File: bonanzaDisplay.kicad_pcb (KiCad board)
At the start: 6 copper layers, 61 x 101 mm, 81 parts, among them J1 OLED-1.31-SSD1322, J15 SWD, J2 Conn_01x02, J5 Conn_01x10, J6 USB_C_Receptacle_USB2.0, SW1 TS-1088-AR02016, SW2 TS-1088-AR02016, SW3 SIQ-02FVS3, U1 RP2354A, U2 XC6206P302MR, U3 XC6206P282MR, U4 TPS62933DRLR, Y1 ABM8-272-T3

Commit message: updated version to v3. switch to 12P FPC
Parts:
- J5: footprint bonanzaDisplay:FPC-SMD_10P-P1.0_FGS-XJ-H2.0 -> bonanzaDisplay:FPC-SMD_12P-P1.00_FGS-XJ-H2.0
- TP22: value SCL -> TX
- TP23: value SDA -> RX
- moved J5 0.97 mm to (118.8, 80.7)
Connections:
- net /DISP_SCL renamed /DISP_TX
- net /DISP_SDA renamed /DISP_RX
- J5 pad 11: GND -> /SWD-DISP
- J5 pad 12: GND -> /SWCLK
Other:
- board text added: "bonanzaDisplay v3"
- board text removed: "bonanzaDisplay v2"

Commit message: rough placements and critical routing done
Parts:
- added TP64: VBUS, bonanzaDisplay:TestPoint_Pad_D1.0mm, B.Cu at (124.5, 33.5)
- J2: moved to B.Cu
- J6: value USB_C_Receptacle_USB2.0 -> TYPE-C-31-M-12; footprint bonanzaDisplay:USB_C_Receptacle_GCT_USB4105-xx-A -> bonanzaDisplay:USB-C_SMD-TYPE-C-31-M-12_1
- moved SW1 84.8 mm to (145.6, 48.0), turned to -90 degrees
- moved R33 82.3 mm to (143.1, 48.1), turned to 90 degrees
- moved SW2 74.5 mm to (137.9, 47.9), turned to -90 degrees
- moved C31 52.6 mm to (136.0, 54.0), turned to 90 degrees
- moved C33 52.0 mm to (137.2, 54.0), turned to 90 degrees
- moved C28 51.3 mm to (140.4, 53.6), turned to 90 degrees
- moved C15 51.0 mm to (141.5, 53.6), turned to 90 degrees
- moved C25 50.5 mm to (143.1, 53.6), turned to 90 degrees
- moved C17 50.4 mm to (131.6, 57.7), turned to 180 degrees
- moved C18 50.3 mm to (144.2, 53.6), turned to 90 degrees
- moved R31 50.1 mm to (145.4, 53.6), turned to 90 degrees
- moved C20 49.8 mm to (133.3, 57.3), turned to 90 degrees
- moved TP17 49.1 mm to (146.9, 53.5), turned to -90 degrees
- moved Y1 47.0 mm to (131.7, 60.5), turned to 90 degrees
- moved L1 46.6 mm to (146.9, 56.0), turned to 90 degrees
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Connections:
- J5 pad 11: /SWD-DISP -> /SWD
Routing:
- net /SW_CCW: track 32.8 -> 82.9 mm, vias 0 -> 2
- net /SW_SW: track 34.0 -> 81.6 mm, vias 0 -> 2
- net /SW_CW: track 36.4 -> 78.0 mm, vias 0 -> 2
- net Net-(J1-IREF): track 2.45 -> 37.7 mm, vias 0 -> 2
- net Net-(J1-VDD): track 2.60 -> 37.1 mm, vias 0 -> 2
- net Net-(J1-VCI): track 2.44 -> 35.6 mm, vias 0 -> 2
- net /2V8: track 16.6 -> 49.2 mm
- net /12V: track 73.3 -> 42.8 mm, vias 5 -> 4
- net Net-(U1-~{QSPI_SS}): track 30.0 -> 0.00 mm, vias 2 -> 0
- net /3V0: track 15.1 -> 44.3 mm, vias 2 -> 4
- net Net-(J1-VSL): track 4.31 -> 33.4 mm, vias 0 -> 2
- net Net-(U1-RUN): track 28.2 -> 0.00 mm, vias 2 -> 0
- net /D6: track 13.1 -> 37.1 mm, vias 0 -> 2
- net /D7: track 13.0 -> 36.9 mm
- net /D5: track 13.1 -> 36.9 mm, vias 0 -> 2
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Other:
- board size 61 x 101 mm -> 30.1 x 89.5 mm

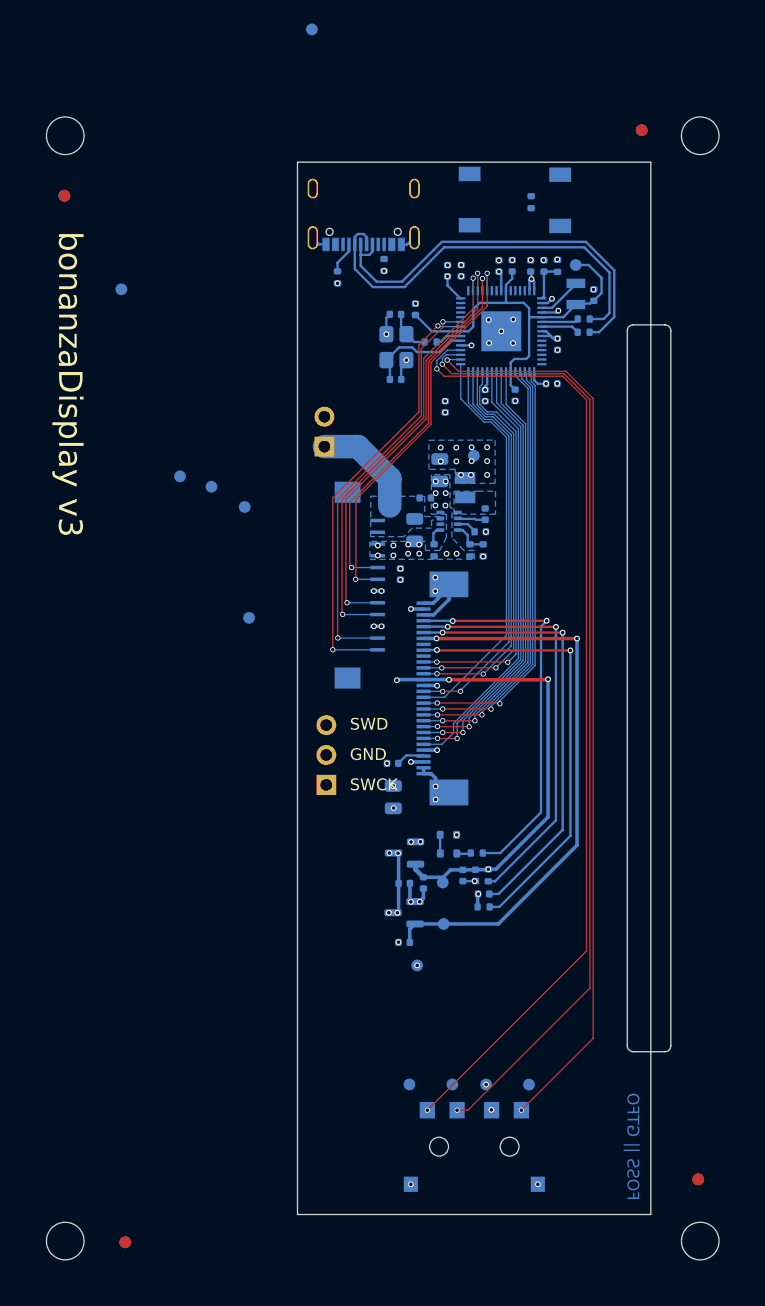
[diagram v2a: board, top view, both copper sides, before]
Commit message: finished routing, DRC and ERC pass
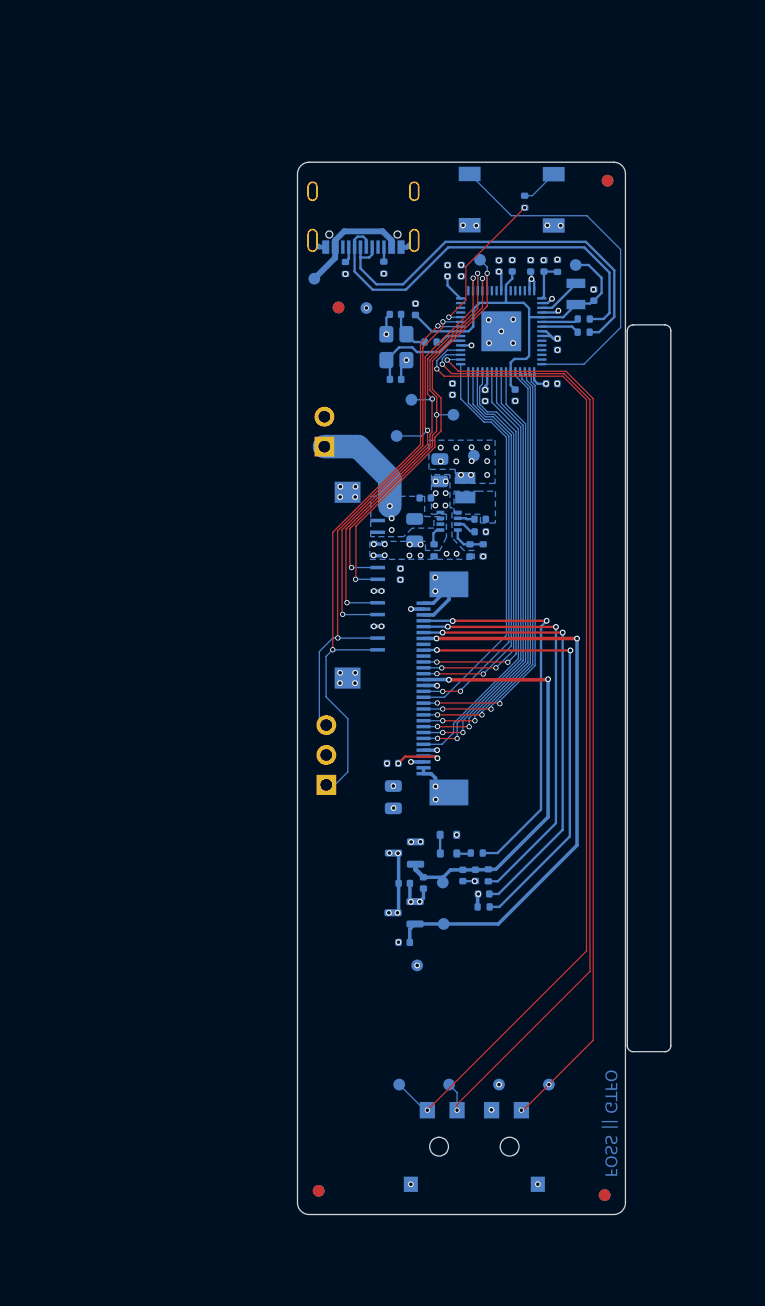
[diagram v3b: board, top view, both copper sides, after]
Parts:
- removed H1, H2, H3, H4: MountingHole_Pad, MountingHole:MountingHole_3.2mm_M3
- moved TP21 30.2 mm to (136.5, 66.2)
- moved TP20 29.0 mm to (138.8, 53.0)
- moved TP19 28.2 mm to (129.1, 57.1)
- moved FID1 25.2 mm to (126.7, 57.1)
- moved TP64 21.2 mm to (124.7, 54.7)
- moved TP23 18.7 mm to (131.7, 68.0), turned to 180 degrees
- moved TP22 18.5 mm to (132.9, 65.0), turned to 180 degrees
- moved FID4 17.0 mm to (125.0, 132.2)
- moved FID3 8.07 mm to (149.4, 132.6)
- moved FID2 5.19 mm to (149.6, 46.3)
- moved TP14 1.69 mm to (144.6, 123.2)
- moved C32 1.62 mm to (136.4, 64.0)
- moved TP24 1.10 mm to (140.4, 123.2)
- moved R2 1.04 mm to (127.3, 53.7)
- moved TP12 0.87 mm to (131.9, 123.2)
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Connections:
- J5 pad 14: unconnected-(J5-Pad14) -> GND
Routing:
- net Net-(U1-~{QSPI_SS}): track 0.00 -> 30.1 mm
- net /SWCLK: track 37.0 -> 50.7 mm
- net Net-(U1-RUN): track 0.00 -> 12.9 mm, vias 0 -> 2
- net Net-(J6-VBUS-PadA4B9): track 0.00 -> 10.0 mm
- net /SWD: track 35.5 -> 44.1 mm
- net /3V0: track 44.3 -> 36.5 mm, vias 4 -> 2
- net /12V: track 42.8 -> 37.1 mm, vias 4 -> 7
- net /SW_CCW: track 82.9 -> 86.2 mm
- net Net-(R33-Pad2): track 0.00 -> 3.23 mm
- net /DISP_RX: track 37.3 -> 40.3 mm, vias 2 -> 3
- net Net-(J1-VCOMH): track 2.45 -> 4.88 mm, vias 0 -> 2
- net /DISP_TX: track 36.8 -> 38.9 mm, vias 2 -> 3
- net /DISP_GPIO2: track 34.0 -> 36.0 mm
- net /SW_SW: track 81.6 -> 83.6 mm
- net /DISP_GPIO1: track 32.6 -> 34.5 mm, vias 2 -> 3
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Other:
- board size 30.1 x 89.5 mm -> 27.9 x 89.5 mm
- board text added: "SWC"
- board text removed: "SWCK"

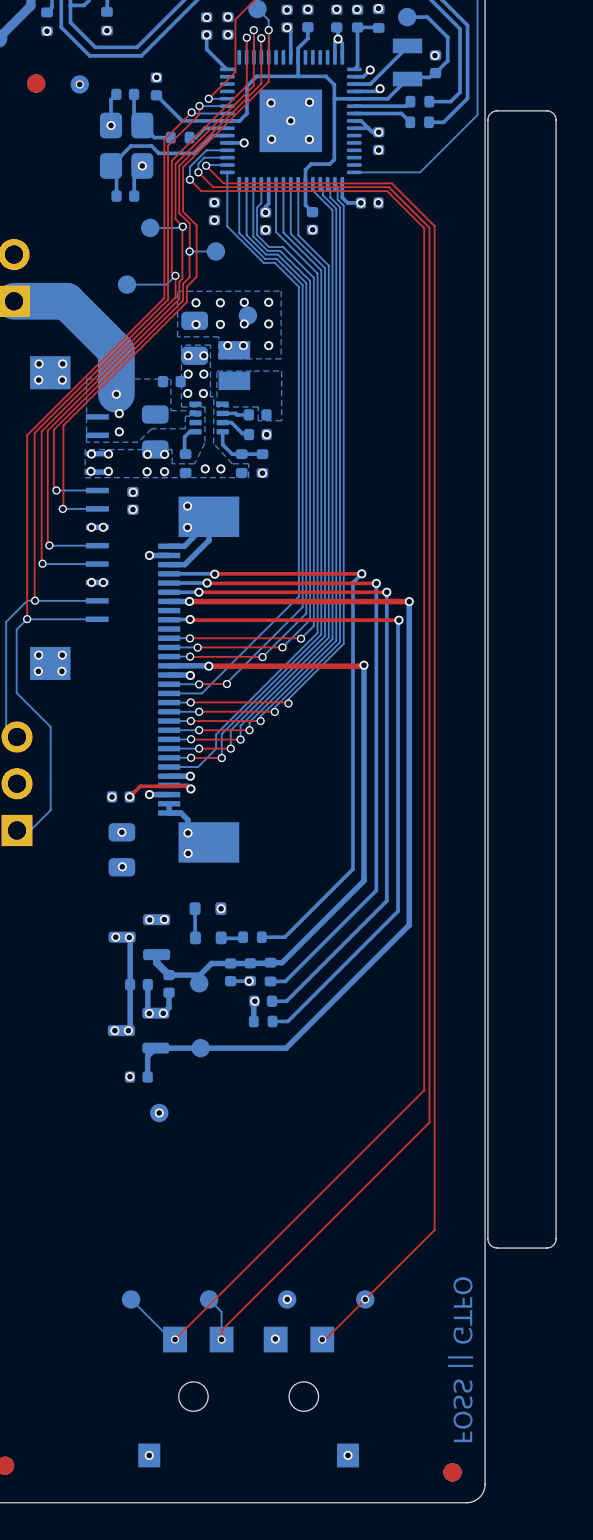
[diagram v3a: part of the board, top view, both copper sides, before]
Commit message: add jlcpcb offsets
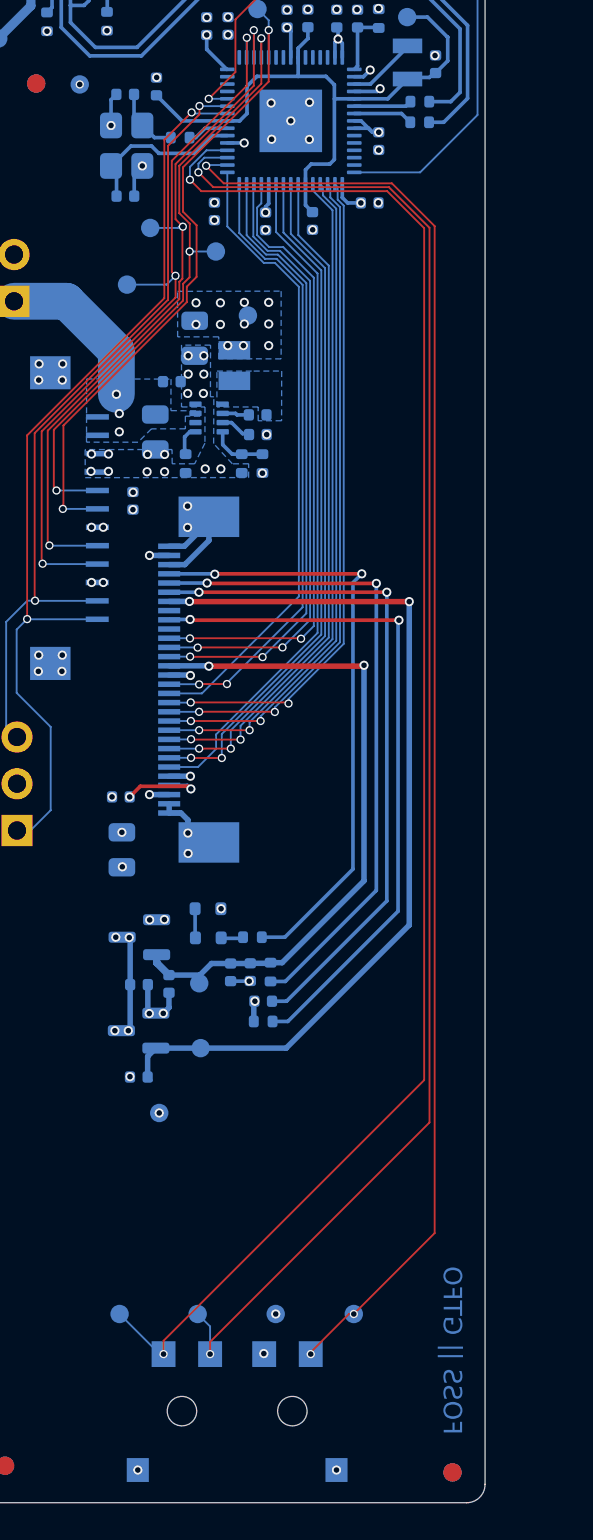
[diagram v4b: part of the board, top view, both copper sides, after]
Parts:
- moved SW3 1.01 mm to (137.7, 129.3)
- moved TP12 1.01 mm to (131.3, 124.0)
- moved TP13 1.01 mm to (135.5, 124.0)
- moved TP14 1.01 mm to (144.0, 124.0)
- moved TP24 1.01 mm to (139.8, 124.0)
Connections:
- net GND renamed /GND
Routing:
- net /SW_CW: track 78.1 -> 79.2 mm
- net /SW_SW: track 83.6 -> 84.6 mm
- net /SW_CCW: track 86.2 -> 87.3 mm

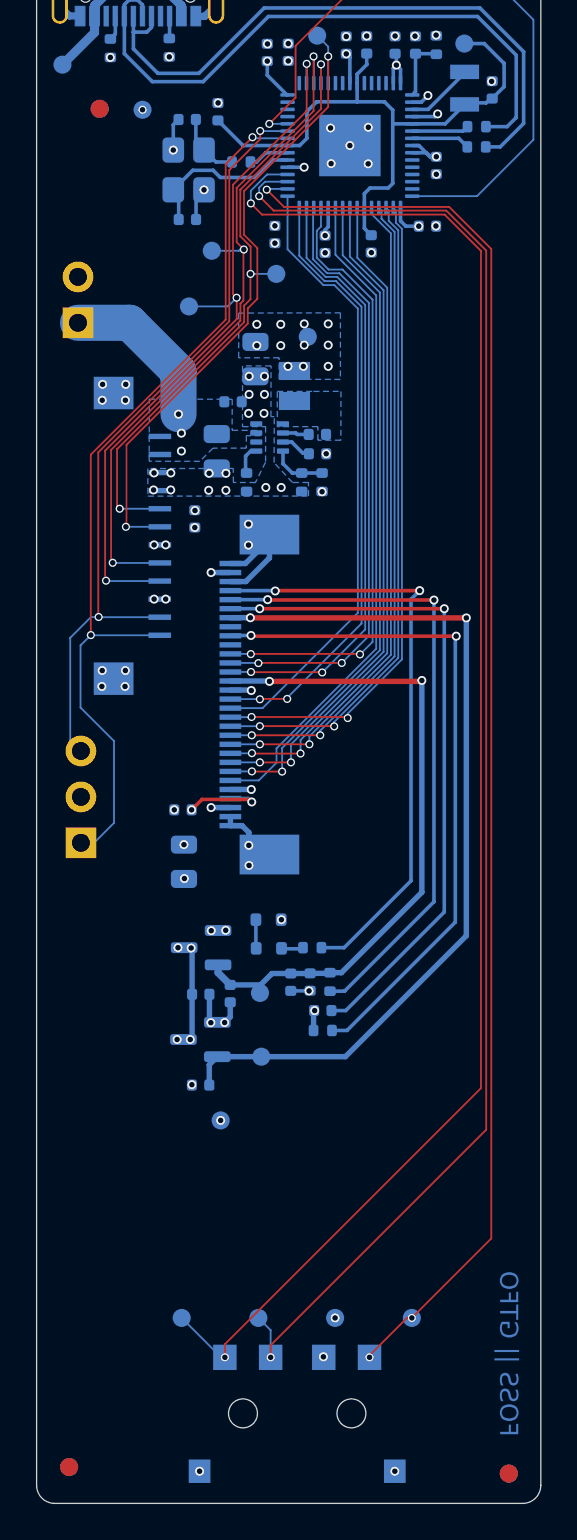
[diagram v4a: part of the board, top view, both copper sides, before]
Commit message: aligned display connector with bitaxeBonanza-1004
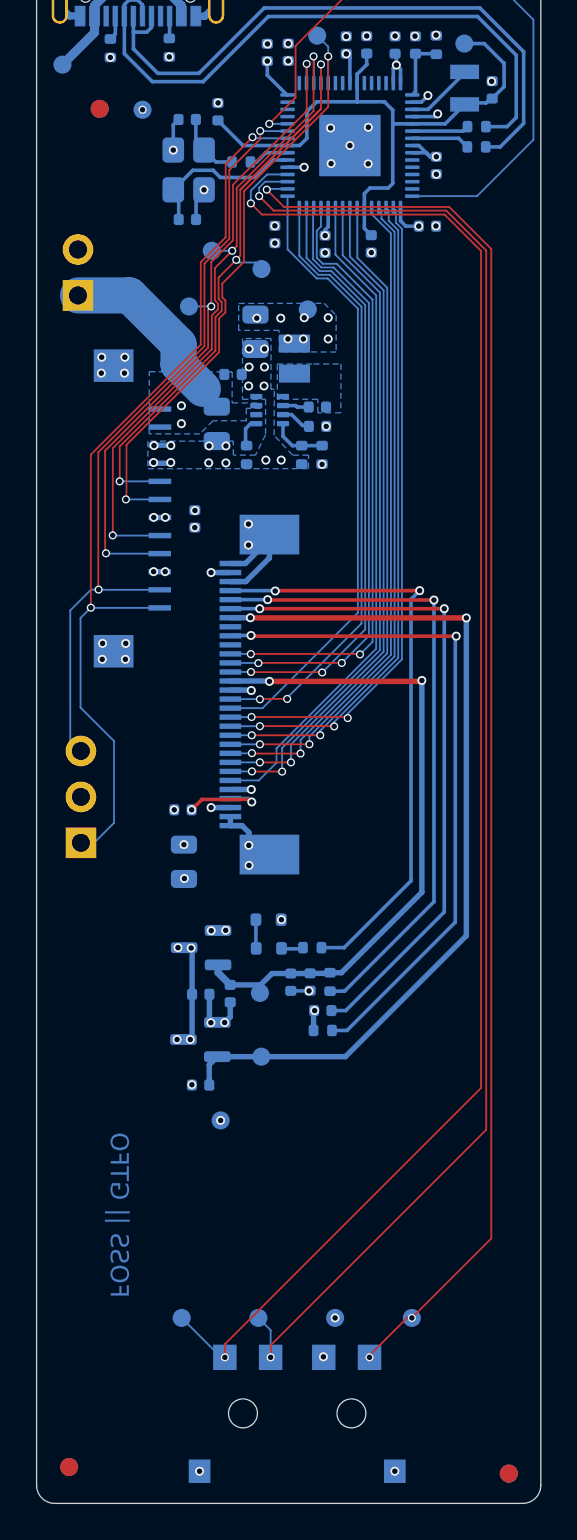
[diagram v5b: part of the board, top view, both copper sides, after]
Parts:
- moved C29 1.52 mm to (138.8, 74.7)
- moved C37 1.52 mm to (134.1, 71.8)
- moved C41 1.52 mm to (138.8, 73.6)
- moved C8 1.52 mm to (133.2, 74.5)
- moved J2 1.52 mm to (125.5, 67.4)
- moved J5 1.52 mm to (128.8, 79.2)
- moved L2 1.52 mm to (137.5, 70.9)
- moved R12 1.52 mm to (139.0, 76.2)
- moved R13 1.52 mm to (137.9, 76.2)
- moved R14 1.52 mm to (134.9, 76.2)
- moved TP9 1.52 mm to (138.2, 68.2)
- moved U4 1.52 mm to (136.1, 73.8)
- moved C34 1.51 mm to (135.4, 69.4)
- moved TP21 0.86 mm to (135.7, 66.0)
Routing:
- net /DISP_GPIO1: track 34.5 -> 39.0 mm
- net /DISP_RX: track 40.3 -> 37.0 mm
- net /DISP_TX: track 38.9 -> 36.6 mm
- net /DISP_GPIO2: track 36.0 -> 34.0 mm
- net /12V: track 37.1 -> 38.6 mm, vias 7 -> 6
- net /3V3: vias 27 -> 23
